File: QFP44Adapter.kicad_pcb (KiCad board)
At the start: 2 copper layers, 57.4 x 21.8 mm, 3 parts, among them J1 Conn_01x22_Male, J2 Conn_01x22_Male, U1 QFP44

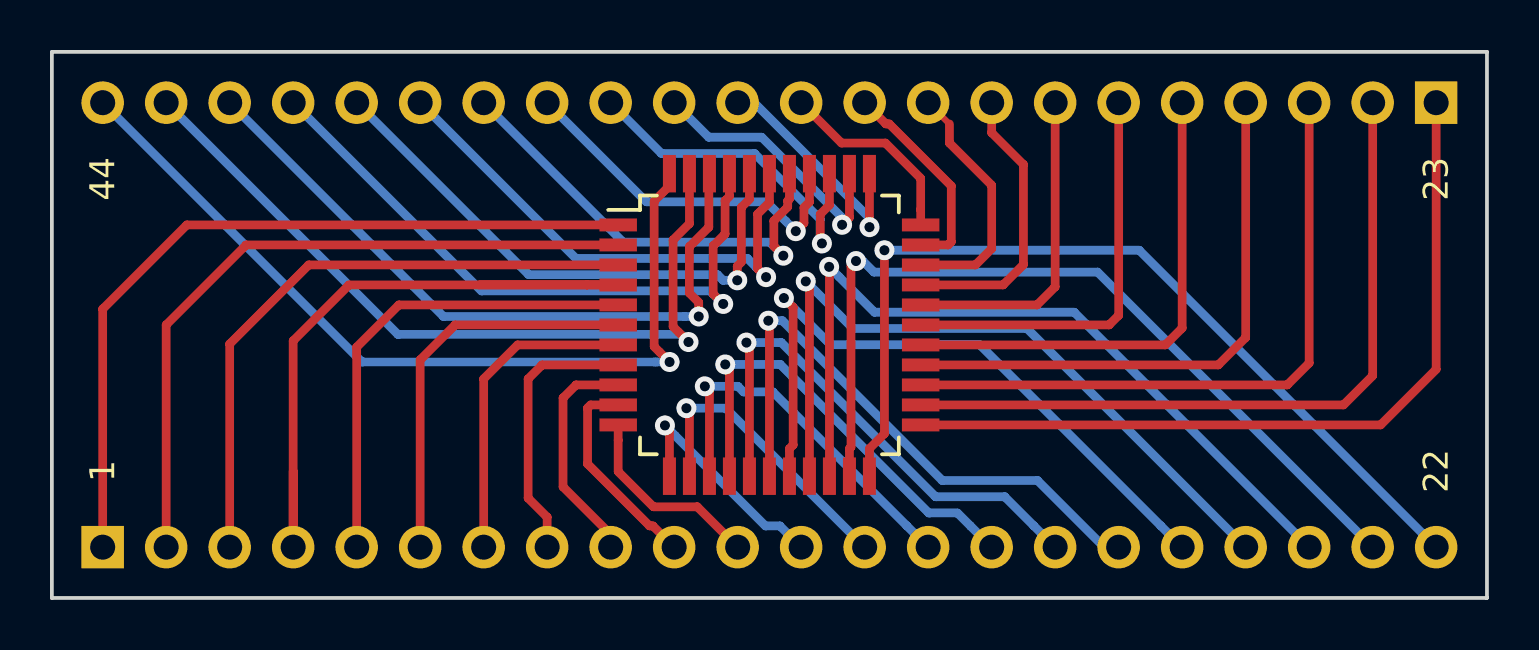
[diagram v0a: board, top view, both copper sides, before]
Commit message: Add KiCAD logo, board title
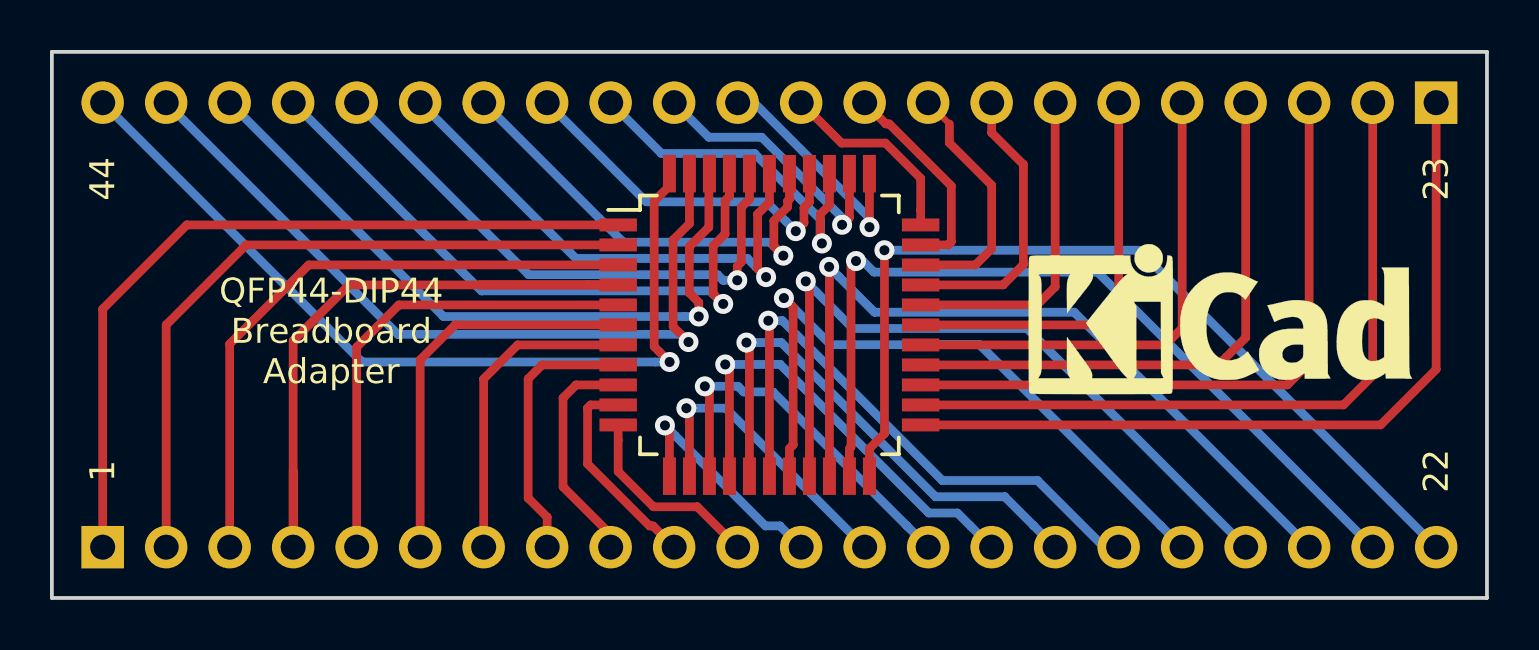
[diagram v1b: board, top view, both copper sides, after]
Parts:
- added REF**: KiCad-Logo_6mm_SilkScreen, Symbol:KiCad-Logo_6mm_SilkScreen, F.Cu at (108.2, 64.5)
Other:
- board text added: "QFP44-DIP44 Breadboard Adapter"
